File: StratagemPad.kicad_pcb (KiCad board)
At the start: 2 copper layers, 6 parts, among them SW1 SW_Push, SW2 SW_Push, SW3 SW_Push, SW4 SW_Push, SW5 SW_Push, U1 XIAO-ESP32-C6-SMD

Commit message: add components + some pcb editing
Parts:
- added D1: LED_BGKR, LED_THT:LED_D5.0mm-4_RGB, F.Cu at (193.4, 113.9)
- added J1: Conn_01x02_Pin, Connector_JST:JST_PH_B2B-PH-K_1x02_P2.00mm_Vertical, F.Cu at (194.6, 106.3)
- added R1: R, Resistor_THT:R_Axial_DIN0204_L3.6mm_D1.6mm_P2.54mm_Vertical, F.Cu at (171.4, 38.1)
- added R2: R, Resistor_THT:R_Axial_DIN0204_L3.6mm_D1.6mm_P2.54mm_Vertical, F.Cu at (187.6, 108.3)
- added R3: R, Resistor_THT:R_Axial_DIN0204_L3.6mm_D1.6mm_P2.54mm_Vertical, F.Cu at (187.6, 111.5)
- moved SW1 58.4 mm to (90.2, 105.6)
- moved SW5 35.5 mm to (147.3, 95.2)
- moved SW2 27.3 mm to (109.2, 95.2)
- moved SW3 20.6 mm to (128.3, 76.2)
- moved SW4 17.2 mm to (128.3, 95.2)
- moved U1 15.3 mm to (166.4, 68.6)
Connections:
- SW1 pad 1: unconnected-(SW1-Pad1) -> /Ground
- SW1 pad 2: unconnected-(SW1-Pad2) -> /Button 1
- SW2 pad 1: unconnected-(SW2-Pad1) -> /Ground
- SW2 pad 2: unconnected-(SW2-Pad2) -> /Button 2
- SW3 pad 1: unconnected-(SW3-Pad1) -> /Ground
- SW3 pad 2: unconnected-(SW3-Pad2) -> /Button 3
- SW4 pad 1: unconnected-(SW4-Pad1) -> /Ground
- SW4 pad 2: unconnected-(SW4-Pad2) -> /Button 4
- SW5 pad 1: unconnected-(SW5-Pad1) -> /Ground
- SW5 pad 2: unconnected-(SW5-Pad2) -> /Button 5
- U1 pad 1: unconnected-(U1-D0-Pad1) -> Net-(U1-D0)
- U1 pad 13: unconnected-(U1-GND-Pad13) -> /Ground
- U1 pad 2: unconnected-(U1-D1-Pad2) -> /LED R
- U1 pad 3: unconnected-(U1-D2-Pad3) -> /LED G
- U1 pad 4: unconnected-(U1-D3-Pad4) -> /LED B
- U1 pad 5: unconnected-(U1-D4-Pad5) -> /Button 1
- U1 pad 6: unconnected-(U1-D5-Pad6) -> /Button 2
- U1 pad 7: unconnected-(U1-D6-Pad7) -> /Button 3
- U1 pad 8: unconnected-(U1-D7-Pad8) -> /Button 4
- U1 pad 9: unconnected-(U1-D8-Pad9) -> /Button 5

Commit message: use global labels + update pcb
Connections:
- net /Button 1 renamed Button 1
- net /Button 2 renamed Button 2
- net /Button 3 renamed Button 3
- net /Button 4 renamed Button 4
- net /Button 5 renamed Button 5
- net /Ground renamed Ground
- net /LED B renamed LED B
- net /LED G renamed LED G
- net /LED R renamed LED R
- net Net-(U1-D0) renamed Battery Read
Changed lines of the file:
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@@
 			(layers "F.Cu" "F.Mask")
 			(roundrect_rratio 0.1)
-			(net "Net-(U1-D0)")
+			(net "Battery Read")
 			(pinfunction "D0_1")
 			(pintype "passive")
@@
 			(layers "*.Cu" "*.Mask")
 			(remove_unused_layers no)
-			(net "Net-(U1-D0)")
+			(net "Battery Read")
 			(pinfunction "D0_1")
 			(pintype "passive")
@@
 			(layers "F.Cu" "F.Mask")
 			(roundrect_rratio 0.1)
-			(net "/LED R")
+			(net "LED R")
 			(pinfunction "D1_2")
 			(pintype "passive")
@@
 			(layers "*.Cu" "*.Mask")
 			(remove_unused_layers no)
-			(net "/LED R")
+			(net "LED R")
 			(pinfunction "D1_2")
 			(pintype "passive")
@@
 			(layers "F.Cu" "F.Mask")
 			(roundrect_rratio 0.1)
-			(net "/LED G")
+			(net "LED G")
 			(pinfunction "D2_3")
 			(pintype "passive")
@@
 			(layers "*.Cu" "*.Mask")
 			(remove_unused_layers no)
-			(net "/LED G")
+			(net "LED G")
 			(pinfunction "D2_3")
 			(pintype "passive")
@@
 			(layers "F.Cu" "F.Mask")
 			(roundrect_rratio 0.1)
-			(net "/LED B")
+			(net "LED B")
 			(pinfunction "D3_4")
 			(pintype "passive")
@@
 			(layers "*.Cu" "*.Mask")
 			(remove_unused_layers no)
-			(net "/LED B")
+			(net "LED B")
 			(pinfunction "D3_4")
 			(pintype "passive")
@@
 			(layers "F.Cu" "F.Mask")
 			(roundrect_rratio 0.1)
-			(net "/Button 1")
+			(net "Button 1")
 			(pinfunction "D4_5")
 			(pintype "passive")
@@
 			(layers "*.Cu" "*.Mask")
 			(remove_unused_layers no)
-			(net "/Button 1")
+			(net "Button 1")
 			(pinfunction "D4_5")
 			(pintype "passive")
@@
 			(layers "F.Cu" "F.Mask")
 			(roundrect_rratio 0.1)
-			(net "/Button 2")
+			(net "Button 2")
 			(pinfunction "D5_6")
 			(pintype "passive")
@@
 			(layers "*.Cu" "*.Mask")
 			(remove_unused_layers no)
-			(net "/Button 2")
+			(net "Button 2")
 			(pinfunction "D5_6")
 			(pintype "passive")
@@
 			(layers "F.Cu" "F.Mask")
 			(roundrect_rratio 0.1)
-			(net "/Button 3")
+			(net "Button 3")
 			(pinfunction "D6_7")
 			(pintype "passive")
@@
 			(layers "*.Cu" "*.Mask")
 			(remove_unused_layers no)
-			(net "/Button 3")
+			(net "Button 3")
 			(pinfunction "D6_7")
 			(pintype "passive")
@@
 			(layers "*.Cu" "*.Mask")
 			(remove_unused_layers no)
-			(net "/Button 4")
+			(net "Button 4")
 			(pinfunction "D7_8")
 			(pintype "passive")
@@
 			(layers "F.Cu" "F.Mask")
 			(roundrect_rratio 0.1)
-			(net "/Button 4")
+			(net "Button 4")
 			(pinfunction "D7_8")
 			(pintype "passive")
@@
 			(layers "*.Cu" "*.Mask")
 			(remove_unused_layers no)
-			(net "/Button 5")
+			(net "Button 5")
 			(pinfunction "D8_9")
 			(pintype "passive")
@@
 			(layers "F.Cu" "F.Mask")
 			(roundrect_rratio 0.1)
-			(net "/Button 5")
+			(net "Button 5")
 			(pinfunction "D8_9")
 			(pintype "passive")
@@
 			(layers "*.Cu" "*.Mask")
 			(remove_unused_layers no)
-			(net "/Ground")
+			(net "Ground")
 			(pinfunction "GND_13")
 			(pintype "passive")
@@
 			(layers "F.Cu" "F.Mask")
 			(roundrect_rratio 0.1)
-			(net "/Ground")
+			(net "Ground")
 			(pinfunction "GND_13")
 			(pintype "passive")
@@
 			(layers "B.Cu" "B.Mask" "B.Paste")
 			(roundrect_rratio 0.1)
-			(net "/Ground")
+			(net "Ground")
 			(pinfunction "1_1")
 			(pintype "passive")
@@
 			(layers "B.Cu" "B.Mask" "B.Paste")
 			(roundrect_rratio 0.1)
-			(net "/Button 2")
+			(net "Button 2")
 			(pinfunction "2_2")
 			(pintype "passive")
@@
 			(layers "*.Cu" "*.Mask")
 			(remove_unused_layers no)
-			(net "/LED B")
+			(net "LED B")
 			(pinfunction "BA_1")
 			(pintype "passive")
@@
 			(layers "*.Cu" "*.Mask")
 			(remove_unused_layers no)
-			(net "/LED G")
+			(net "LED G")
 			(pinfunction "GA_2")
 			(pintype "passive")
@@
 			(layers "*.Cu" "*.Mask")
 			(remove_unused_layers no)
-			(net "/LED R")
+			(net "LED R")
 			(pinfunction "RA_4")
 			(pintype "passive")
@@
 			(layers "B.Cu" "B.Mask" "B.Paste")
 			(roundrect_rratio 0.1)
-			(net "/Ground")
+			(net "Ground")
 			(pinfunction "1_1")
 			(pintype "passive")
@@
 			(layers "B.Cu" "B.Mask" "B.Paste")
 			(roundrect_rratio 0.1)
-			(net "/Button 4")
+			(net "Button 4")
 			(pinfunction "2_2")
 			(pintype "passive")
@@
 			(layers "*.Cu" "*.Mask")
 			(remove_unused_layers no)
-			(net "/Ground")
+			(net "Ground")
 			(pintype "passive")
 		)
@@
 			(layers "*.Cu" "*.Mask")
 			(remove_unused_layers no)
-			(net "Net-(U1-D0)")
+			(net "Battery Read")
 			(pintype "passive")
 		)
@@
 			(layers "*.Cu" "*.Mask")
 			(remove_unused_layers no)
-			(net "Net-(U1-D0)")
+			(net "Battery Read")
 			(pintype "passive")
 		)
@@
 			(layers "B.Cu" "B.Mask" "B.Paste")
 			(roundrect_rratio 0.1)
-			(net "/Ground")
+			(net "Ground")
 			(pinfunction "1_1")
 			(pintype "passive")
@@
 			(layers "B.Cu" "B.Mask" "B.Paste")
 			(roundrect_rratio 0.1)
-			(net "/Button 3")
+			(net "Button 3")
 			(pinfunction "2_2")
 			(pintype "passive")
@@
 			(layers "B.Cu" "B.Mask" "B.Paste")
 			(roundrect_rratio 0.1)
-			(net "/Ground")
+			(net "Ground")
 			(pinfunction "1_1")
 			(pintype "passive")
@@
 			(layers "B.Cu" "B.Mask" "B.Paste")
 			(roundrect_rratio 0.1)
-			(net "/Button 1")
+			(net "Button 1")
 			(pinfunction "2_2")
 			(pintype "passive")
@@
 			(layers "B.Cu" "B.Mask" "B.Paste")
 			(roundrect_rratio 0.1)
-			(net "/Ground")
+			(net "Ground")
 			(pinfunction "1_1")
 			(pintype "passive")
@@
 			(layers "B.Cu" "B.Mask" "B.Paste")
 			(roundrect_rratio 0.1)
-			(net "/Button 5")
+			(net "Button 5")
 			(pinfunction "2_2")
 			(pintype "passive")

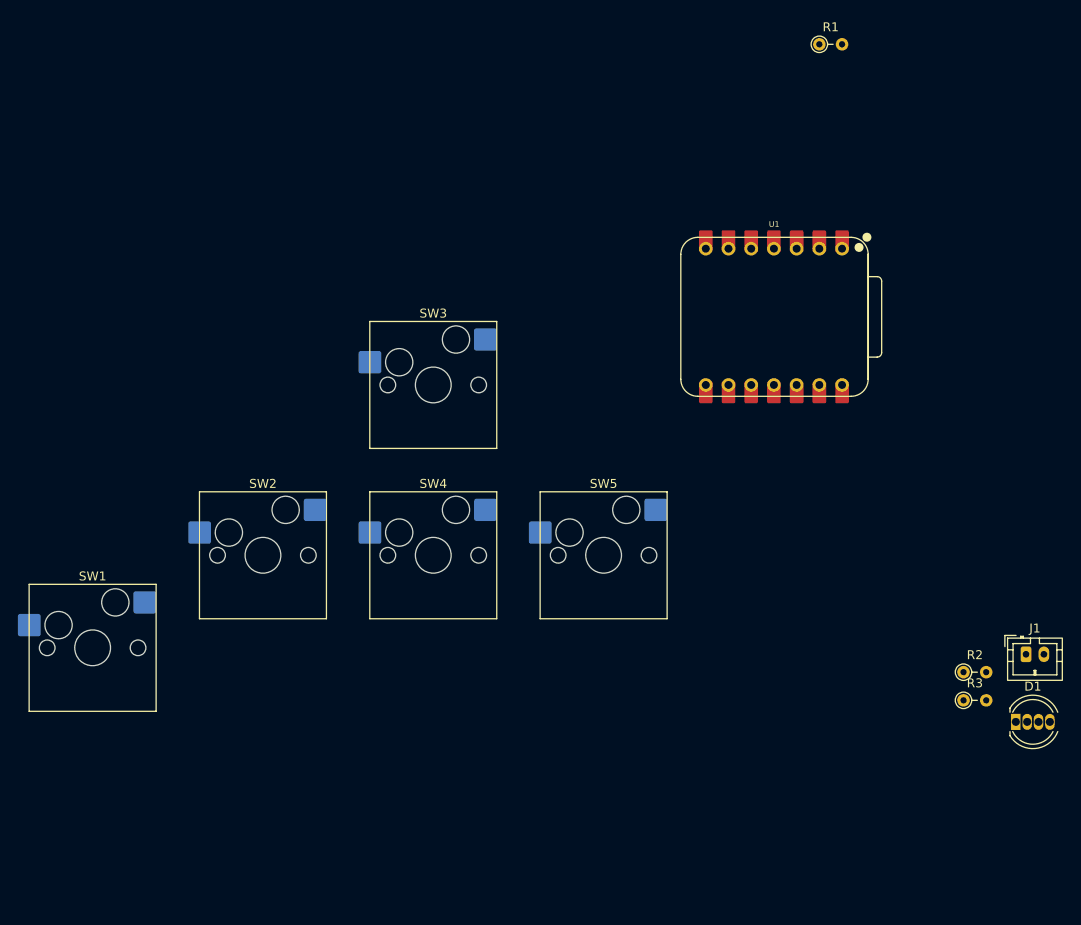
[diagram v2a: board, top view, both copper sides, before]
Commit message: set pcb origin point + move with reference
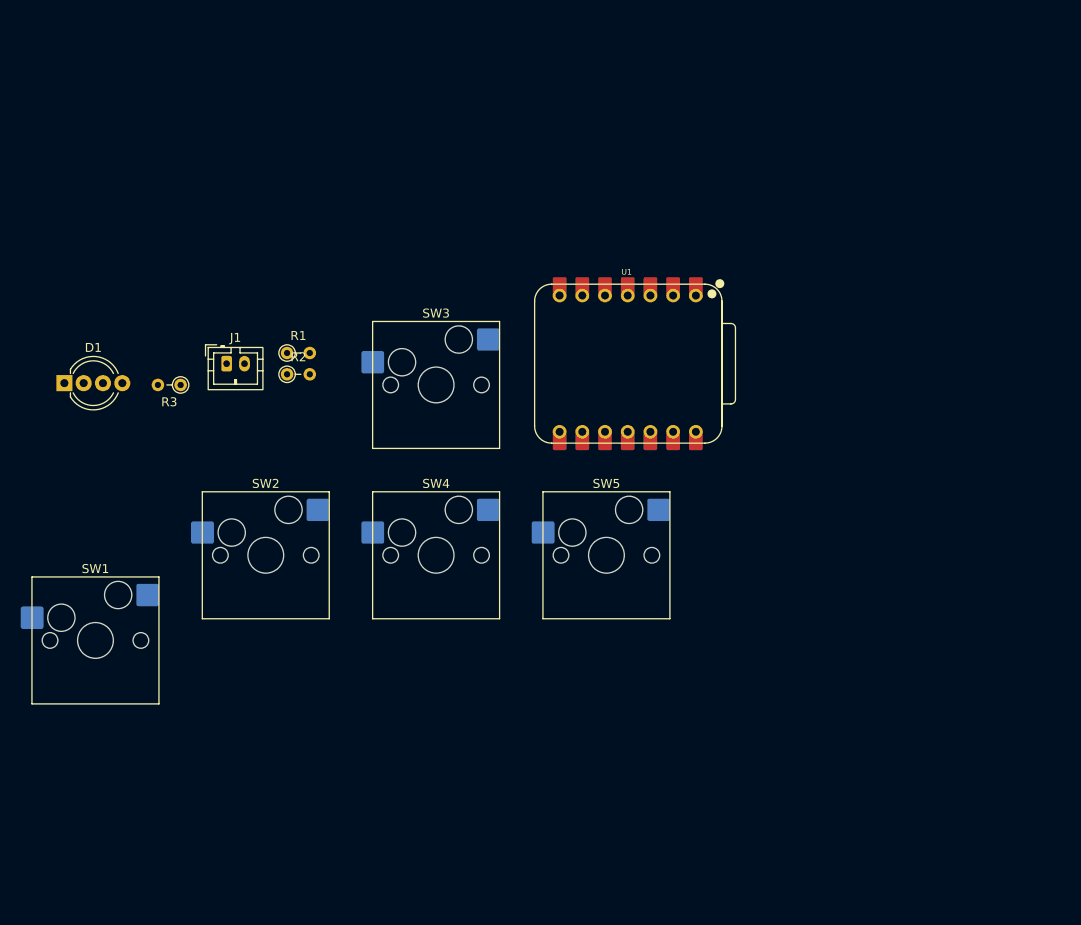
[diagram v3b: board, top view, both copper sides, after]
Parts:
- D1: footprint LED_THT:LED_D5.0mm-4_RGB -> LED_THT:LED_D5.0mm-4_RGB_Wide_Pins
- U1: footprint Seeed_Studio_XIAO_Series:XIAO-ESP32-S3-DIP -> Seeed_Studio_XIAO_Series:XIAO-ESP32-C6-DIP
- moved D1 113.0 mm to (87.0, 76.0)
- moved J1 95.1 mm to (105.2, 73.8)
- moved R3 94.4 mm to (100.0, 76.2), turned to 180 degrees
- moved R2 82.7 mm to (111.9, 75.0)
- moved R1 68.8 mm to (111.9, 72.6)
- moved U1 17.2 mm to (150.0, 73.8)
- moved SW1 0.88 mm to (90.5, 104.8)
- moved SW2 0.32 mm to (109.5, 95.2)
- moved SW3 0.32 mm to (128.6, 76.2)
- moved SW4 0.32 mm to (128.6, 95.2)
- moved SW5 0.32 mm to (147.6, 95.2)
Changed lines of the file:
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@@
 		)
 	)
-	(footprint "Seeed_Studio_XIAO_Series:XIAO-ESP32-S3-DIP"
+	(footprint "Seeed_Studio_XIAO_Series:XIAO-ESP32-C6-DIP"
 		(layer "F.Cu")
-		(at 166.37 68.58)
+		(at 150.01875 73.81875)
 		(property "Reference" "U1"
-			(at 0.025 -10.35 0)
+			(at -0.125 -10.25 0)
 			(unlocked yes)
 			(layer "F.SilkS")
@@
 		)
 		(property "Value" "XIAO-ESP32-C6-SMD"
-			(at 0.8185 0 0)
+			(at 0 0 0)
 			(unlocked yes)
 			(layer "F.Fab")
@@
 		)
 		(fp_circle
-			(center 9.52 -7.761)
-			(end 9.774 -7.761)
+			(center 9.42 -7.807)
+			(end 9.674 -7.807)
 			(stroke
 				(width 0.5)
@@
 		)
 		(fp_circle
-			(center 10.4 -8.904)
-			(end 10.654 -8.904)
+			(center 10.3 -8.95)
+			(end 10.554 -8.95)
 			(stroke
 				(width 0.5)
@@
 		)
 		(fp_circle
-			(center 9.526 -7.758)
-			(end 9.78 -7.758)
+			(center 9.426 -7.804)
+			(end 9.68 -7.804)
 			(stroke
 				(width 0.5)
@@
 	(footprint "PCM_Switch_Keyboard_Hotswap_Kailh:SW_Hotswap_Kailh_MX_1.00u"
 		(layer "F.Cu")
-		(at 109.22 95.25)
+		(at 109.5375 95.25)
 		(descr "Kailh keyswitch Hotswap Socket Keycap 1.00u")
 		(tags "Kailh Keyboard Keyswitch Switch Hotswap Socket Relief Cutout Keycap 1.00u")
@@
 		)
 	)
-	(footprint "LED_THT:LED_D5.0mm-4_RGB"
+	(footprint "LED_THT:LED_D5.0mm-4_RGB_Wide_Pins"
 		(layer "F.Cu")
-		(at 193.425 113.885)
-		(descr "LED, RGB, diameter 5.0mm, 4 pins, https://www.kingbright.com/attachments/file/psearch/000/00/00/L-154A4SUREQBFZGEW(Ver.13A).pdf, generated by kicad-footprint-generator")
-		(tags "LED")
+		(at 87.01 76)
+		(descr "LED, diameter 5.0mm, 4 pins, WP154A4, https://www.kingbright.com/attachments/file/psearch/000/00/00/L-154A4SUREQBFZGEW(Ver.11A).pdf")
+		(tags "LED diameter 5.0mm 2 pins diameter 5.0mm 3 pins diameter 5.0mm 4 pins RGB RGBLED")
 		(property "Reference" "D1"
-			(at 1.905 -3.96 0)
+			(at 3.2385 -3.96 0)
 			(layer "F.SilkS")
 			(effects
@@
 		)
 		(property "Value" "LED_BGKR"
-			(at 1.905 3.96 0)
+			(at 3.2385 3.96 0)
 			(layer "F.Fab")
 			(effects
@@
 		(property "Datasheet" ""
 			(at 0 0 0)
+			(unlocked yes)
 			(layer "F.Fab")
 			(hide yes)
@@
 				(font
 					(size 1.27 1.27)
+					(thickness 0.15)
 				)
 			)
@@
 		(property "Description" "RGB LED, blue/green/cathode/red"
 			(at 0 0 0)
+			(unlocked yes)
 			(layer "F.Fab")
 			(hide yes)
@@
 				(font
 					(size 1.27 1.27)
-				)
-			)
-		)
-		(property "KiLib_Generator" "LED/THT"
-			(at 0 0 0)
-			(layer "F.SilkS")
-			(hide yes)
-			(effects
-				(font
-					(size 1 1)
 					(thickness 0.15)
 				)
@@
 		(duplicate_pad_numbers_are_jumpers no)
 		(fp_line
-			(start -0.655 -1.545)
-			(end -0.655 -1.08)
+			(start 0.6785 -1.545)
+			(end 0.6785 -1.08)
 			(stroke
 				(width 0.12)
@@
 		)
 		(fp_line
-			(start -0.655 1.08)
-			(end -0.655 1.545)
+			(start 0.6785 1.08)
+			(end 0.6785 1.545)
 			(stroke
 				(width 0.12)
@@
 		)
 		(fp_arc
-			(start -0.655 -1.54483)
-			(mid 2.163898 -2.97877)
-			(end 4.693136 -1.08)
+			(start 0.6785 -1.54483)
+			(mid 3.496956 -2.978809)
+			(end 6.026315 -1.080827)
 			(stroke
 				(width 0.12)
@@
 		)
 		(fp_arc
-			(start -0.349684 -1.08)
-			(mid 1.905 -2.5)
-			(end 4.159684 -1.08)
+			(start 0.983816 -1.08)
+			(mid 3.238262 -2.5)
+			(end 5.492979 -1.080429)
 			(stroke
 				(width 0.12)
@@
 		)
 		(fp_arc
-			(start 4.159684 1.08)
-			(mid 1.905 2.5)
-			(end -0.349684 1.08)
+			(start 5.492979 1.080429)
+			(mid 3.238262 2.5)
+			(end 0.983816 1.08)
 			(stroke
 				(width 0.12)
@@
 		)
 		(fp_arc
-			(start 4.693136 1.08)
-			(mid 2.163898 2.97877)
-			(end -0.655 1.54483)
+			(start 6.026315 1.080827)
+			(mid 3.496956 2.978808)
+			(end 0.6785 1.54483)
 			(stroke
 				(width 0.12)
@@
 			(layer "F.SilkS")
 		)
-		(fp_rect
-			(start -1.31 -3.21)
-			(end 5.12 3.21)
+		(fp_line
+			(start -1.08 -3.25)
+			(end -1.08 3.25)
+			(stroke
+				(width 0.05)
+				(type solid)
+			)
+			(layer "F.CrtYd")
+		)
+		(fp_line
+			(start -1.08 3.25)
+			(end 7.56 3.25)
+			(stroke
+				(width 0.05)
+				(type solid)
+			)
+			(layer "F.CrtYd")
+		)
+		(fp_line
+			(start 7.56 -3.25)
+			(end -1.08 -3.25)
 			(stroke
 				(width 0.05)
 				(type solid)
 			)
-			(fill no)
 			(layer "F.CrtYd")
 		)
 		(fp_line
-			(start -0.595 -1.469694)
-			(end -0.595 1.469694)
+			(start 7.56 3.25)
+			(end 7.56 -3.25)
+			(stroke
+				(width 0.05)
+				(type solid)
+			)
+			(layer "F.CrtYd")
+		)
+		(fp_line
+			(start 0.7385 -1.469694)
+			(end 0.7385 1.469694)
 			(stroke
 				(width 0.1)
@@
 		)
 		(fp_arc
-			(start -0.595 -1.469694)
-			(mid 4.805 0)
-			(end -0.595 1.469694)
+			(start 0.7385 -1.469694)
+			(mid 6.1385 0.000016)
+			(end 0.738484 1.469666)
 			(stroke
 				(width 0.1)
@@
 		)
 		(fp_circle
-			(center 1.905 0)
-			(end 4.405 0)
+			(center 3.2385 0)
+			(end 5.7385 0)
 			(stroke
 				(width 0.1)
@@
 		)
 		(fp_text user "${REFERENCE}"
-			(at 1.905 0 0)
+			(at 3.2385 -3.96 0)
 			(layer "F.Fab")
 			(effects
 				(font
-					(size 0.8 0.8)
-					(thickness 0.12)
+					(size 1 1)
+					(thickness 0.15)
 				)
 			)
 		)
-		(point
-			(at 195.33 113.885)
-			(size 2)
-			(layer "F.Fab")
-		)
 		(pad "1" thru_hole rect
 			(at 0 0)
-			(size 1.07 1.8)
+			(size 1.8 1.8)
 			(drill 0.9)
 			(layers "*.Cu" "*.Mask")
@@
 			(pintype "passive")
 		)
-		(pad "2" thru_hole oval
-			(at 1.27 0)
-			(size 1.07 1.8)
+		(pad "2" thru_hole circle
+			(at 2.159 0)
+			(size 1.8 1.8)
 			(drill 0.9)
 			(layers "*.Cu" "*.Mask")
@@
 			(pintype "passive")
 		)
-		(pad "3" thru_hole oval
-			(at 2.54 0)
-			(size 1.07 1.8)
+		(pad "3" thru_hole circle
+			(at 4.318 0)
+			(size 1.8 1.8)
 			(drill 0.9)
 			(layers "*.Cu" "*.Mask")
@@
 			(pintype "passive")
 		)
-		(pad "4" thru_hole oval
-			(at 3.81 0)
-			(size 1.07 1.8)
+		(pad "4" thru_hole circle
+			(at 6.477 0)
+			(size 1.8 1.8)
 			(drill 0.9)
 			(layers "*.Cu" "*.Mask")
@@
 		)
 		(embedded_fonts no)
-		(model "${KICAD10_3DMODEL_DIR}/LED_THT.3dshapes/LED_D5.0mm-4_RGB.step"
+		(model "${KICAD10_3DMODEL_DIR}/LED_THT.3dshapes/LED_D5.0mm-4_RGB_Wide_Pins.step"
 			(offset
 				(xyz 0 0 0)
@@
 	(footprint "PCM_Switch_Keyboard_Hotswap_Kailh:SW_Hotswap_Kailh_MX_1.00u"
 		(layer "F.Cu")
-		(at 128.27 95.25)
+		(at 128.5875 95.25)
 		(descr "Kailh keyswitch Hotswap Socket Keycap 1.00u")
 		(tags "Kailh Keyboard Keyswitch Switch Hotswap Socket Relief Cutout Keycap 1.00u")
@@
 	(footprint "Resistor_THT:R_Axial_DIN0204_L3.6mm_D1.6mm_P2.54mm_Vertical"
 		(layer "F.Cu")
-		(at 187.575 111.475)
+		(at 100.0125 76.2 180)
 		(descr "Resistor, Axial_DIN0204 series, Axial, Vertical, pin pitch=2.54mm, 0.167W, length*diameter=3.6*1.6mm^2, http://cdn-reichelt.de/documents/datenblatt/B400/1_4W%23YAG.pdf")
 		(tags "Resistor Axial_DIN0204 series Axial Vertical pin pitch 2.54mm 0.167W length 3.6mm diameter 1.6mm")
@@
 		)
 		(pad "1" thru_hole circle
-			(at 0 0)
+			(at 0 0 180)
 			(size 1.4 1.4)
 			(drill 0.7)
@@
 		)
 		(pad "2" thru_hole circle
-			(at 2.54 0)
+			(at 2.54 0 180)
 			(size 1.4 1.4)
 			(drill 0.7)
@@
 	(footprint "Resistor_THT:R_Axial_DIN0204_L3.6mm_D1.6mm_P2.54mm_Vertical"
 		(layer "F.Cu")
-		(at 171.45 38.1)
+		(at 111.91875 72.628125)
 		(descr "Resistor, Axial_DIN0204 series, Axial, Vertical, pin pitch=2.54mm, 0.167W, length*diameter=3.6*1.6mm^2, http://cdn-reichelt.de/documents/datenblatt/B400/1_4W%23YAG.pdf")
 		(tags "Resistor Axial_DIN0204 series Axial Vertical pin pitch 2.54mm 0.167W length 3.6mm diameter 1.6mm")
@@
 	(footprint "Resistor_THT:R_Axial_DIN0204_L3.6mm_D1.6mm_P2.54mm_Vertical"
 		(layer "F.Cu")
-		(at 187.575 108.325)
+		(at 111.91875 75.009375)
 		(descr "Resistor, Axial_DIN0204 series, Axial, Vertical, pin pitch=2.54mm, 0.167W, length*diameter=3.6*1.6mm^2, http://cdn-reichelt.de/documents/datenblatt/B400/1_4W%23YAG.pdf")
 		(tags "Resistor Axial_DIN0204 series Axial Vertical pin pitch 2.54mm 0.167W length 3.6mm diameter 1.6mm")
@@
 	(footprint "Connector_JST:JST_PH_B2B-PH-K_1x02_P2.00mm_Vertical"
 		(layer "F.Cu")
-		(at 194.565 106.325)
+		(at 105.15625 73.81875)
 		(descr "JST PH series connector, B2B-PH-K (http://www.jst-mfg.com/product/pdf/eng/ePH.pdf)")
 		(tags "connector JST PH vertical")
@@
 	(footprint "PCM_Switch_Keyboard_Hotswap_Kailh:SW_Hotswap_Kailh_MX_1.00u"
 		(layer "F.Cu")
-		(at 128.27 76.2)
+		(at 128.5875 76.2)
 		(descr "Kailh keyswitch Hotswap Socket Keycap 1.00u")
 		(tags "Kailh Keyboard Keyswitch Switch Hotswap Socket Relief Cutout Keycap 1.00u")
@@
 	(footprint "PCM_Switch_Keyboard_Hotswap_Kailh:SW_Hotswap_Kailh_MX_1.50u_90deg"
 		(layer "F.Cu")
-		(at 90.17 105.6)
+		(at 90.4875 104.775)
 		(descr "Kailh keyswitch Hotswap Socket Keycap 1.50u 90deg")
 		(tags "Kailh Keyboard Keyswitch Switch Hotswap Socket Relief Cutout Keycap 1.50u 90deg")
@@
 	(footprint "PCM_Switch_Keyboard_Hotswap_Kailh:SW_Hotswap_Kailh_MX_1.00u"
 		(layer "F.Cu")
-		(at 147.32 95.25)
+		(at 147.6375 95.25)
 		(descr "Kailh keyswitch Hotswap Socket Keycap 1.00u")
 		(tags "Kailh Keyboard Keyswitch Switch Hotswap Socket Relief Cutout Keycap 1.00u")
@@
 		)
 	)
+	(point
+		(at 80.9625 90.4875)
+		(size 1)
+		(layer "F.SilkS")
+	)
+	(point
+		(at 80.9625 90.4875)
+		(size 1)
+		(layer "F.SilkS")
+	)
 	(embedded_fonts no)
